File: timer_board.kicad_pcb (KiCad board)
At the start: 2 copper layers, 127 x 76.2 mm, 53 parts, among them IC1 ATMEGA32U4, K1 T9AS5D22-5, P1 USBMICRO, P2 OUT_INV, P3 Trigger, P4 OUT, Q1 NPN, Q2 NPN, U1 DS3231MZ, U2 74HC04, Y1 RESONATORSMD

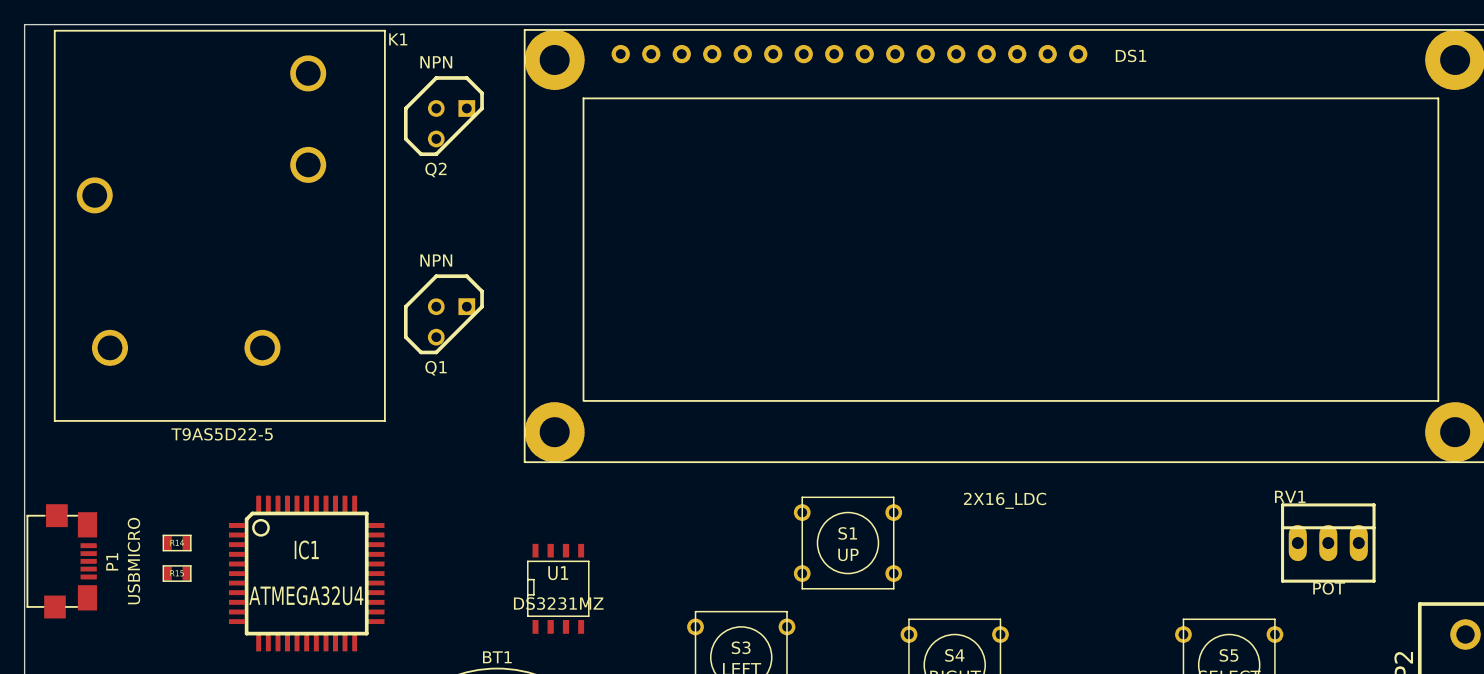
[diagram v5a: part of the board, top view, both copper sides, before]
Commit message: Added Pot
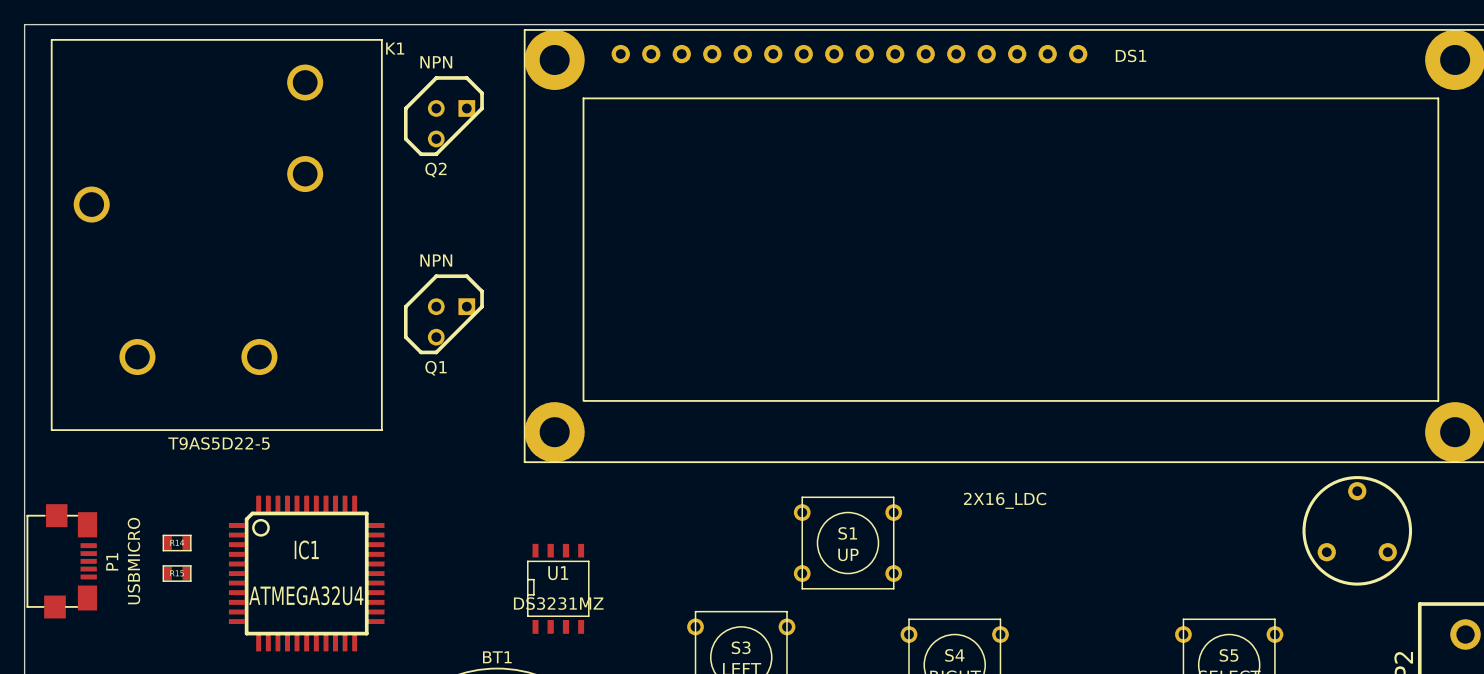
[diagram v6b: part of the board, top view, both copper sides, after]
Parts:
- RV1: footprint PINHEAD1-3 -> Var_resistor
- moved RV1 3.00 mm to (136.4, 66.8)
- moved K1 0.80 mm to (41.7, 42.7)
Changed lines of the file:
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@@
-    )
-  )
-  (module PINHEAD1-3 (layer F.Cu)
-    (at 133.985 68.58)
-    (attr virtual)
-    (fp_text reference RV1 (at -3.175 -3.81) (layer F.SilkS)
-      (effects (font (size 1.016 1.016) (thickness 0.0889)))
-    )
-    (fp_text value POT (at 0 3.81) (layer F.SilkS)
-      (effects (font (size 1.016 1.016) (thickness 0.0889)))
-    )
-    (fp_line (start -3.81 -3.175) (end -3.81 3.175) (layer F.SilkS) (width 0.254))
-    (fp_line (start 3.81 -3.175) (end 3.81 3.175) (layer F.SilkS) (width 0.254))
-    (fp_line (start 3.81 -1.27) (end -3.81 -1.27) (layer F.SilkS) (width 0.254))
-    (fp_line (start -3.81 -3.175) (end 3.81 -3.175) (layer F.SilkS) (width 0.254))
-    (fp_line (start 3.81 3.175) (end -3.81 3.175) (layer F.SilkS) (width 0.254))
-    (pad 1 thru_hole oval (at -2.54 0) (size 1.50622 3.01498) (drill 0.99822)
-      (layers *.Cu F.Paste F.SilkS F.Mask)
-      (net 1 +5V)
-    )
-    (pad 2 thru_hole oval (at 0 0) (size 1.50622 3.01498) (drill 0.99822)
-      (layers *.Cu F.Paste F.SilkS F.Mask)
-      (net 31 N-000044)
-    )
-    (pad 3 thru_hole oval (at 2.54 0) (size 1.50622 3.01498) (drill 0.99822)
-      (layers *.Cu F.Paste F.SilkS F.Mask)
-      (net 9 GND)
     )
   )
@@
     )
   )
-  (module T9AS5D22-5 (layer F.Cu)
-    (at 41.91 41.91)
-    (fp_text reference K1 (at 14.605 -15.24) (layer F.SilkS)
-      (effects (font (size 1 1) (thickness 0.15)))
-    )
-    (fp_text value T9AS5D22-5 (at 0 17.653) (layer F.SilkS)
-      (effects (font (size 1 1) (thickness 0.15)))
-    )
-    (fp_line (start -14 -16) (end 13.5 -16) (layer F.SilkS) (width 0.15))
-    (fp_line (start 13.5 -16) (end 13.5 16.5) (layer F.SilkS) (width 0.15))
-    (fp_line (start 13.5 16.5) (end -14 16.5) (layer F.SilkS) (width 0.15))
-    (fp_line (start -14 16.5) (end -14 -16) (layer F.SilkS) (width 0.15))
-    (pad 5 thru_hole circle (at 7.112 -12.446) (size 3 3) (drill 2.06)
-      (layers *.Cu *.Mask F.SilkS)
-    )
-    (pad 4 thru_hole circle (at 7.112 -4.826) (size 3 3) (drill 2.06)
-      (layers *.Cu *.Mask F.SilkS)
-    )
-    (pad 1 thru_hole circle (at -10.668 -2.286) (size 3 3) (drill 2.06)
-      (layers *.Cu *.Mask F.SilkS)
-    )
-    (pad 3 thru_hole circle (at 3.302 10.414) (size 3 3) (drill 2.06)
-      (layers *.Cu *.Mask F.SilkS)
-      (net 15 N-000015)
-    )
-    (pad 2 thru_hole circle (at -9.398 10.414) (size 3 3) (drill 2.06)
-      (layers *.Cu *.Mask F.SilkS)
-      (net 1 +5V)
-    )
-  )
   (module RESONATOR-SMD (layer F.Cu)
     (at 48.26 81.28)
@@
       (rotate (xyz 0 0 0))
     )
+  )
+  (module T9AS5D22-5 (layer F.Cu)
+    (at 41.656 42.672)
+    (fp_text reference K1 (at 14.605 -15.24) (layer F.SilkS)
+      (effects (font (size 1 1) (thickness 0.15)))
+    )
+    (fp_text value T9AS5D22-5 (at 0 17.653) (layer F.SilkS)
+      (effects (font (size 1 1) (thickness 0.15)))
+    )
+    (fp_line (start -14 -16) (end 13.5 -16) (layer F.SilkS) (width 0.15))
+    (fp_line (start 13.5 -16) (end 13.5 16.5) (layer F.SilkS) (width 0.15))
+    (fp_line (start 13.5 16.5) (end -14 16.5) (layer F.SilkS) (width 0.15))
+    (fp_line (start -14 16.5) (end -14 -16) (layer F.SilkS) (width 0.15))
+    (pad 5 thru_hole circle (at 7.112 -12.446) (size 3 3) (drill 2.06)
+      (layers *.Cu *.Mask F.SilkS)
+    )
+    (pad 4 thru_hole circle (at 7.112 -4.826) (size 3 3) (drill 2.06)
+      (layers *.Cu *.Mask F.SilkS)
+    )
+    (pad 1 thru_hole circle (at -10.668 -2.286) (size 3 3) (drill 2.06)
+      (layers *.Cu *.Mask F.SilkS)
+    )
+    (pad 3 thru_hole circle (at 3.302 10.414) (size 3 3) (drill 2.06)
+      (layers *.Cu *.Mask F.SilkS)
+      (net 15 N-000015)
+    )
+    (pad 2 thru_hole circle (at -6.858 10.414) (size 3 3) (drill 2.06)
+      (layers *.Cu *.Mask F.SilkS)
+      (net 1 +5V)
+    )
+  )
+  (module Var_resistor (layer F.Cu)
+    (at 136.398 66.802)
+    (descr "Resistance variable / potentiometre")
+    (tags R)
+    (autoplace_cost90 10)
+    (autoplace_cost180 10)
+    (fp_text reference RV1 (at 0 -0.381) (layer F.SilkS) hide
+      (effects (font (size 1.397 1.27) (thickness 0.2032)))
+    )
+    (fp_text value POT (at 0 3.81) (layer F.SilkS) hide
+      (effects (font (size 1.397 1.27) (thickness 0.2032)))
+    )
+    (fp_circle (center 0 0.762) (end 4.318 1.778) (layer F.SilkS) (width 0.254))
+    (pad 1 thru_hole circle (at -2.54 2.54) (size 1.524 1.524) (drill 0.8128)
+      (layers *.Cu *.Mask F.SilkS)
+      (net 1 +5V)
+    )
+    (pad 2 thru_hole circle (at 0 -2.54) (size 1.524 1.524) (drill 0.8128)
+      (layers *.Cu *.Mask F.SilkS)
+      (net 31 N-000044)
+    )
+    (pad 3 thru_hole circle (at 2.54 2.54) (size 1.524 1.524) (drill 0.8128)
+      (layers *.Cu *.Mask F.SilkS)
+      (net 9 GND)
+    )
+    (model discret/adjustable_rx2.wrl
+      (at (xyz 0 0 0))
+      (scale (xyz 1 1 1))
+      (rotate (xyz 0 0 0))
+    )

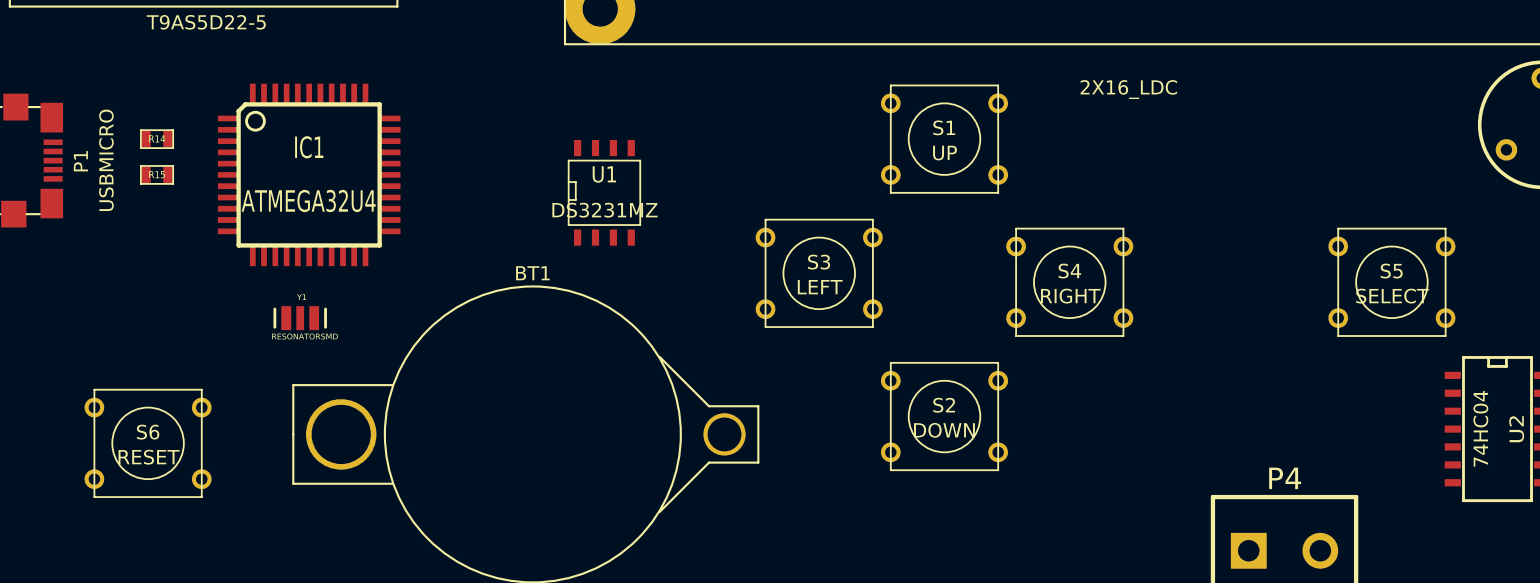
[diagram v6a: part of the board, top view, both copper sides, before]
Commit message: Modified Push button
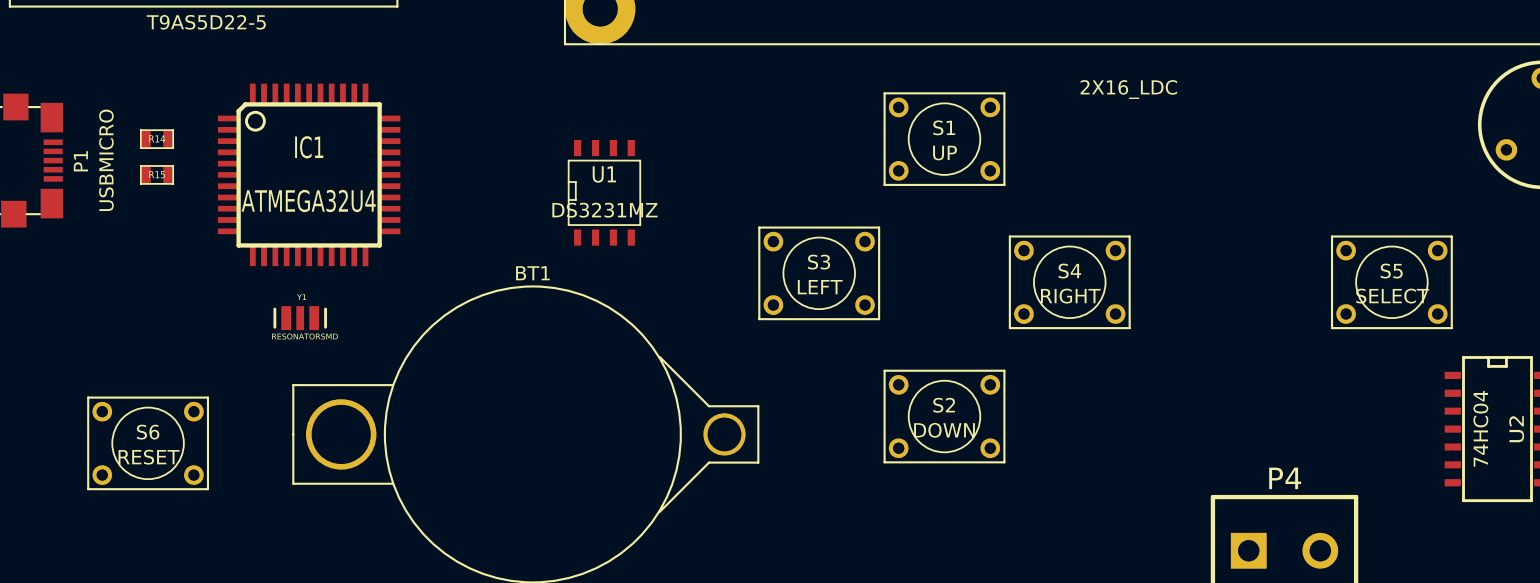
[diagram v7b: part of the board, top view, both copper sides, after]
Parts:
- S1, S2, S3, S4, S5, S6: footprint SW_PUSH_SMALL -> SW_PUSH_6X6
